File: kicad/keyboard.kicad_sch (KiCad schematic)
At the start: 8 parts, among them SW1 SW_Push, U1 Arduino_pro_Micro

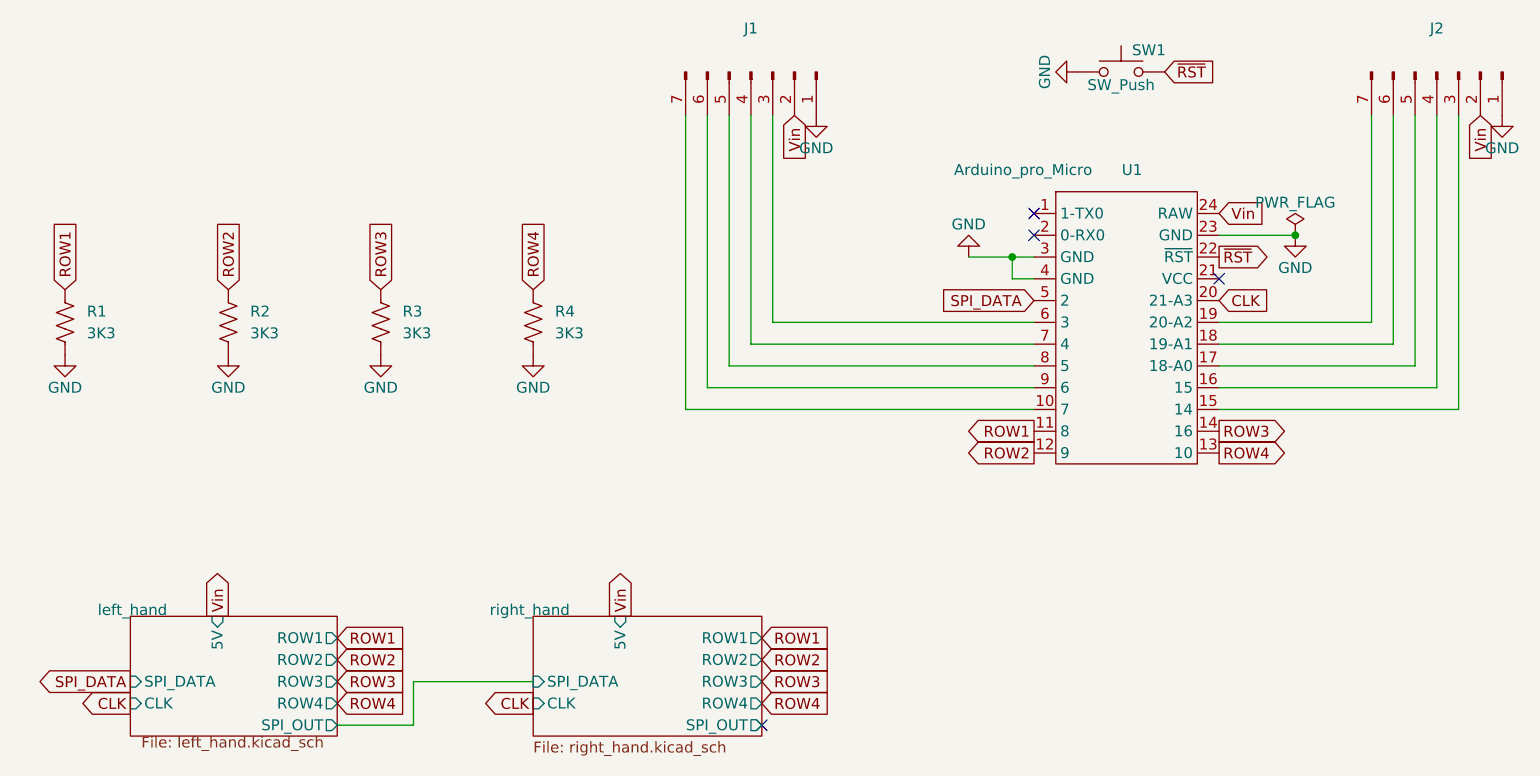
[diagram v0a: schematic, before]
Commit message: Update switch diode
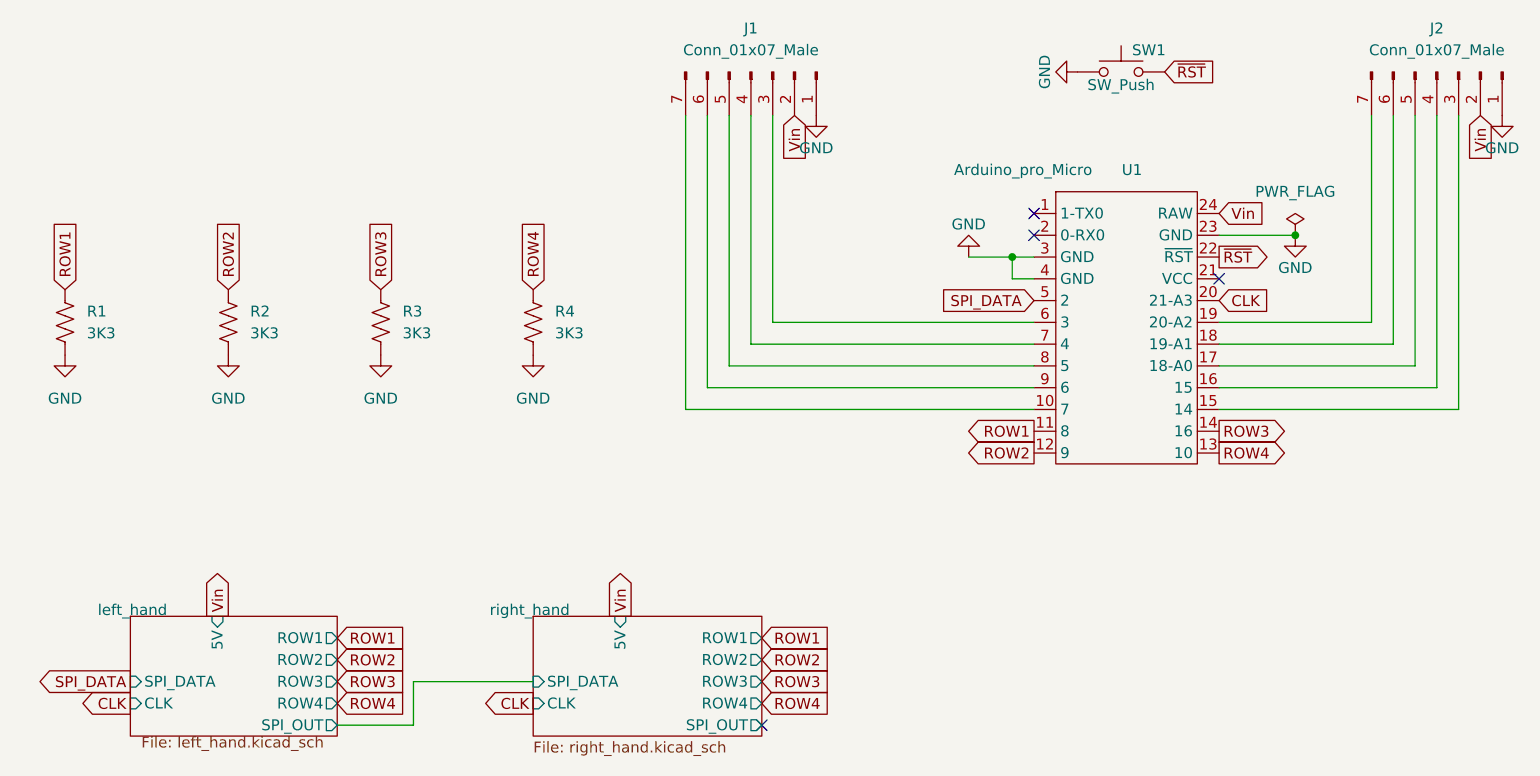
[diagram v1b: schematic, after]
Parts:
- J1, J2: value (none) -> Conn_01x07_Male; footprint (none) -> Keyboard:PinHeader_01x07; symbol Connector:Conn_01x07_Male -> Connector:Conn_01x07_Pin

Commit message: Update PCB
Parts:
- added D59: LED, LED_SMD:LED_0805_2012Metric, symbol Device:LED
- added R5: 220R, Resistor_SMD:R_0603_1608Metric, symbol Device:R_US
- J1: footprint Keyboard:PinHeader_01x07 -> Connector_PinHeader_2.54mm:PinHeader_1x05_P2.54mm_Vertical; symbol Connector:Conn_01x07_Pin -> Connector:Conn_01x05_Pin; now not fitted
- J2, SW1, U1: now not fitted
- R1, R2, R3, R4: footprint Resistor_THT:R_Axial_DIN0207_L6.3mm_D2.5mm_P7.62mm_Horizontal -> Resistor_SMD:R_0603_1608Metric; LCSC (none) -> C22978
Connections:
- net ROW1: now also U1.9 (6); no longer U1.11 (8)
- net ROW2: now also U1.10 (7); no longer U1.12 (9)
- net ROW3: now also U1.11 (8); no longer U1.14 (16)
- net ROW4: now also U1.12 (9); no longer U1.13 (10)
- net Vin: now also D59.2 (A)
- net ~{RST}: now also J2.3 (Pin_3)
- net MISO: now reaches U1.15 (14)
- net MISO: now also J2.5 (Pin_5); no longer J2.3 (Pin_3)
- net MOSI: now reaches J2.4 (Pin_4)
- net MOSI: now also U1.14 (16); no longer U1.16 (15)
- net at U1.17 (18-A0): no longer J2.5 (Pin_5)
- net at U1.18 (19-A1): no longer J2.6 (Pin_6)
- new net: R5.1, U1.13 (10)
- new net: D59.1 (K), R5.2
- new net SCLK: J2.6 (Pin_6), U1.16 (15)
- no-connect marks 4 -> 6
